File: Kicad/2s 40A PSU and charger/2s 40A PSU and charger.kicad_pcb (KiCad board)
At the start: 4 copper layers, 45 x 20 mm, 117 parts, among them J1 Keystone 3579, J10 USB_C_Receptacle_USB2.0_16P, J11 1.27mm 4 pin socket, J12 USB, J2 JST XH-S Balance Plug, J3 Keystone 3579, J4 Keystone 3569, J5 Keystone 3569, J6 Keystone 3579, J7 Keystone 3579, J8 Keystone 3569, J9 Keystone 3569, Q1 PJA3430, Q2 PJA3430, Q3 Vishay sir404dp, or SiR500DP, Q4 PJA3430, Q5 PJA3430, Q6 Vishay sir404dp, or SiR500DP, U1 BQ76905RGRR, U2 AP63203WU, U3 BQ24780SRUYR, U4 TLV709A33DBVR, U5 THVD1420DRLR, U6 CH32X035G8U6

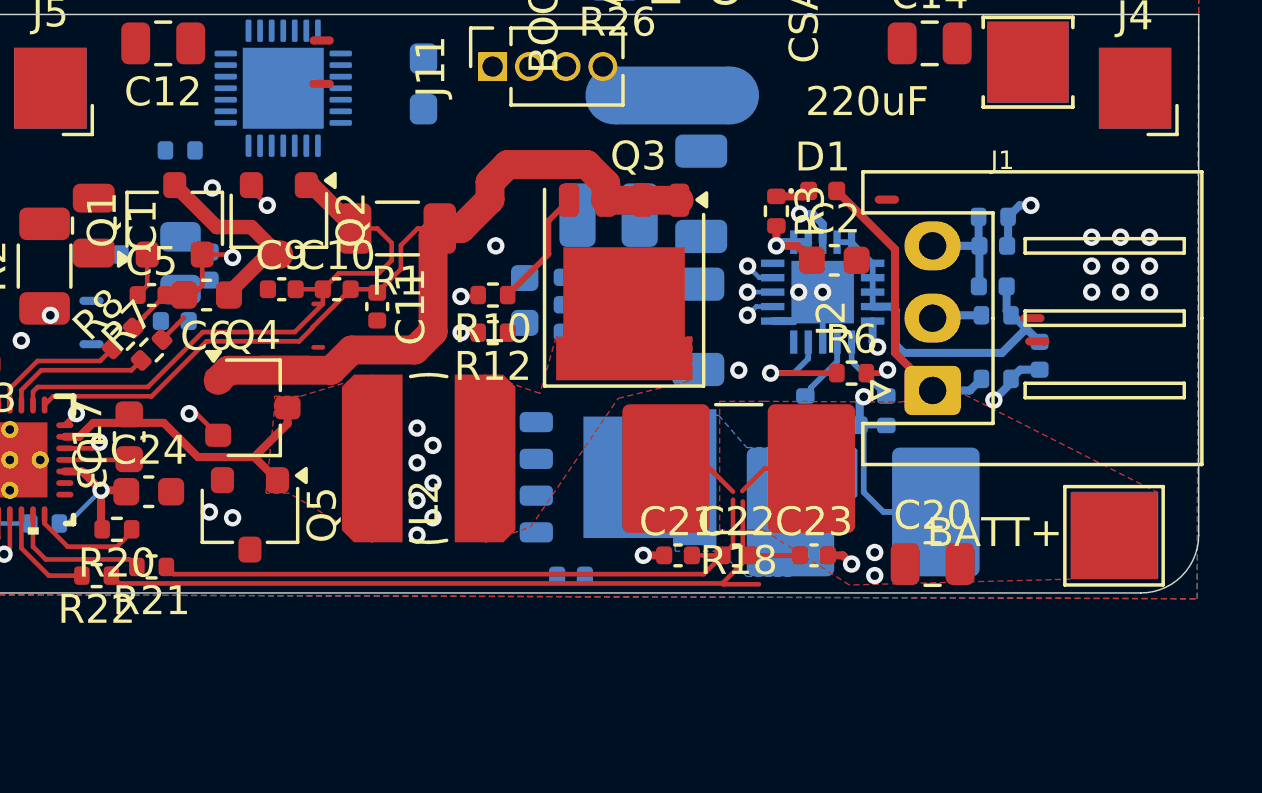
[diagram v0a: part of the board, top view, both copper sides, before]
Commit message: Changed battery input pads to through holes with vias
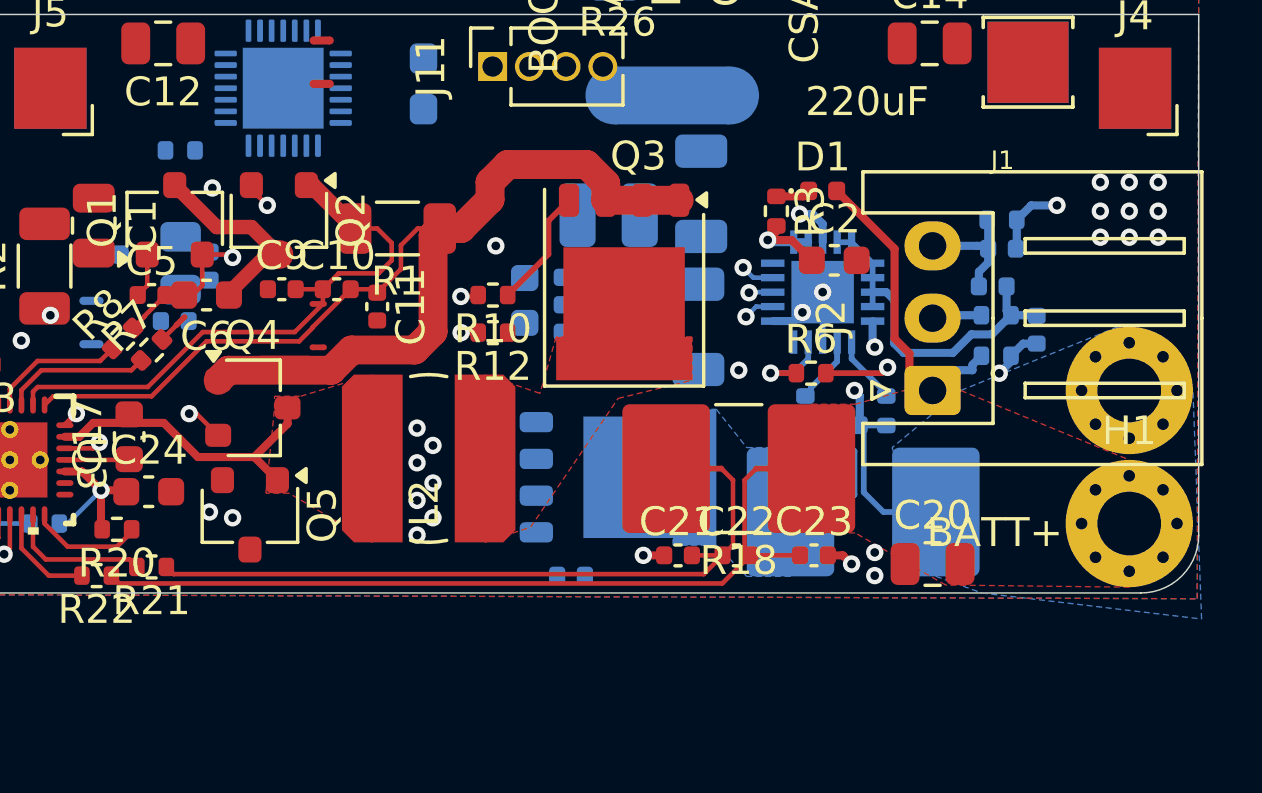
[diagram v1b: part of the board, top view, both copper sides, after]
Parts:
- H1, H2: footprint TestPoint:TestPoint_Pad_3.0x3.0mm -> MountingHole:MountingHole_2.2mm_M2_Pad_Via
- NT14, NT2, NT3, NT5, NT6: footprint custom_Connector:NetTie-2_SMD_Pad0.16mm -> custom_Connector:NetTie-2_SMD_Pad0.2mm
- NT7, NT8: moved to B.Cu
- moved NT9 5.65 mm to (143.1, 124.0), turned to 90 degrees
- moved H2 5.02 mm to (150.7, 125.0), turned to -45 degrees
- moved NT7 3.33 mm to (145.2, 120.0), turned to 180 degrees
- moved NT8 2.71 mm to (145.0, 124.3), turned to 180 degrees
- moved NT5 1.46 mm to (138.0, 127.7), turned to 0 degrees
- moved R6 1.40 mm to (139.7, 124.4)
- moved NT6 1.38 mm to (136.4, 127.7), turned to 180 degrees
- moved C13 0.91 mm to (147.5, 122.9)
- moved R15 0.80 mm to (146.1, 123.8)
- moved H1 0.68 mm to (150.7, 129.6)
- moved C19 0.32 mm to (146.3, 120.1)
- moved R17 0.32 mm to (146.3, 119.1)
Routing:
- net /Battery Balancer/-BAT: track 0.00 -> 23.1 mm, vias 0 -> 1
- net Net-(C18-Pad2): track 25.6 -> 2.87 mm, vias 1 -> 0
- net (no net): track 10.3 -> 0.15 mm
- net Net-(D1-A): track 0.00 -> 6.66 mm
- net /Battery Balancer/+BAT: track 2.72 -> 0.00 mm
- net Net-(Q3-S): track 2.64 -> 0.00 mm
- net Net-(C21-Pad2): track 22.4 -> 24.0 mm
- net /Battery Balancer/Low: track 13.6 -> 15.0 mm
- net Net-(Q6-G): track 0.78 -> 2.22 mm
- net Net-(U1-DSG): track 4.37 -> 2.97 mm
- net Net-(NT8-Pad1): track 0.00 -> 0.63 mm
- net Net-(U1-BAT): track 3.27 -> 3.86 mm
- net /Battery Balancer/Up: track 16.9 -> 17.5 mm
- added copper zone on B.Cu, net /Battery Balancer/-BAT
- added copper zone on B.Cu, net Net-(Q6-S)
- removed copper zone on B.Cu, net (none)

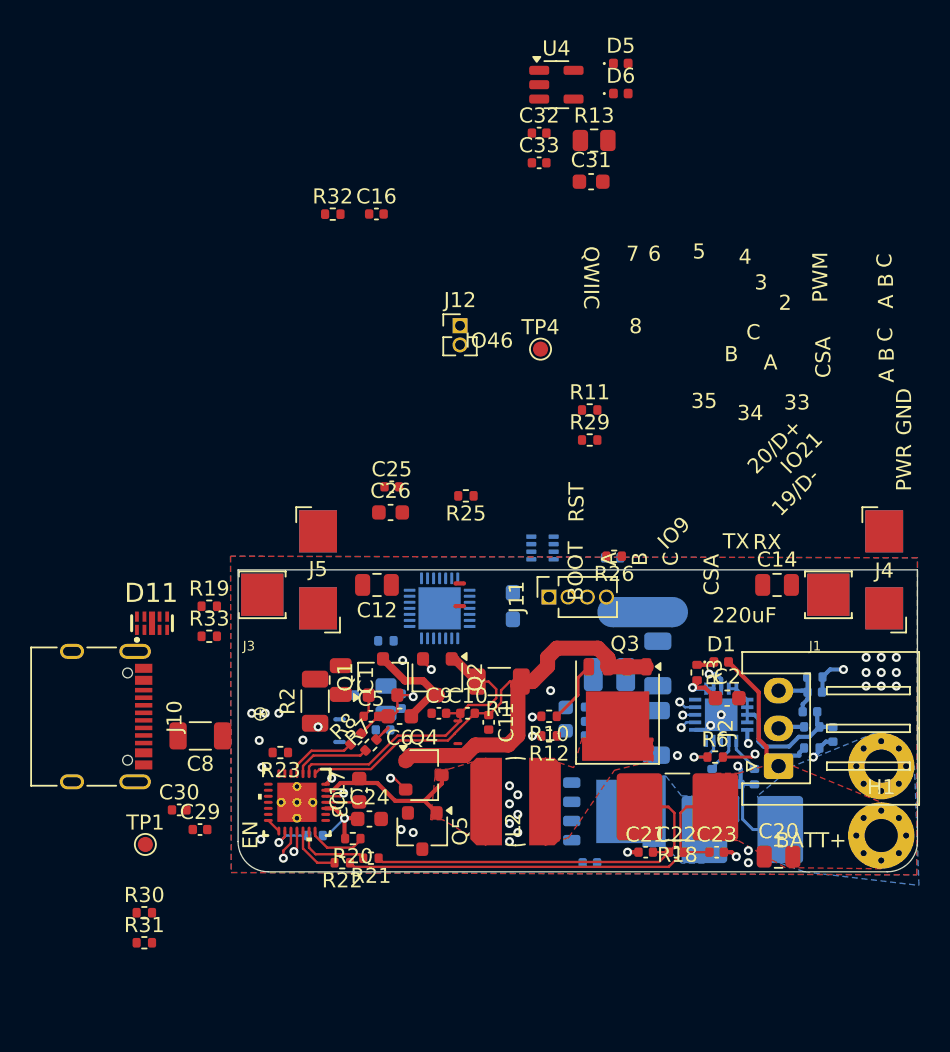
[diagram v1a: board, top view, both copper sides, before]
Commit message: Added TVS diodes for USB-C
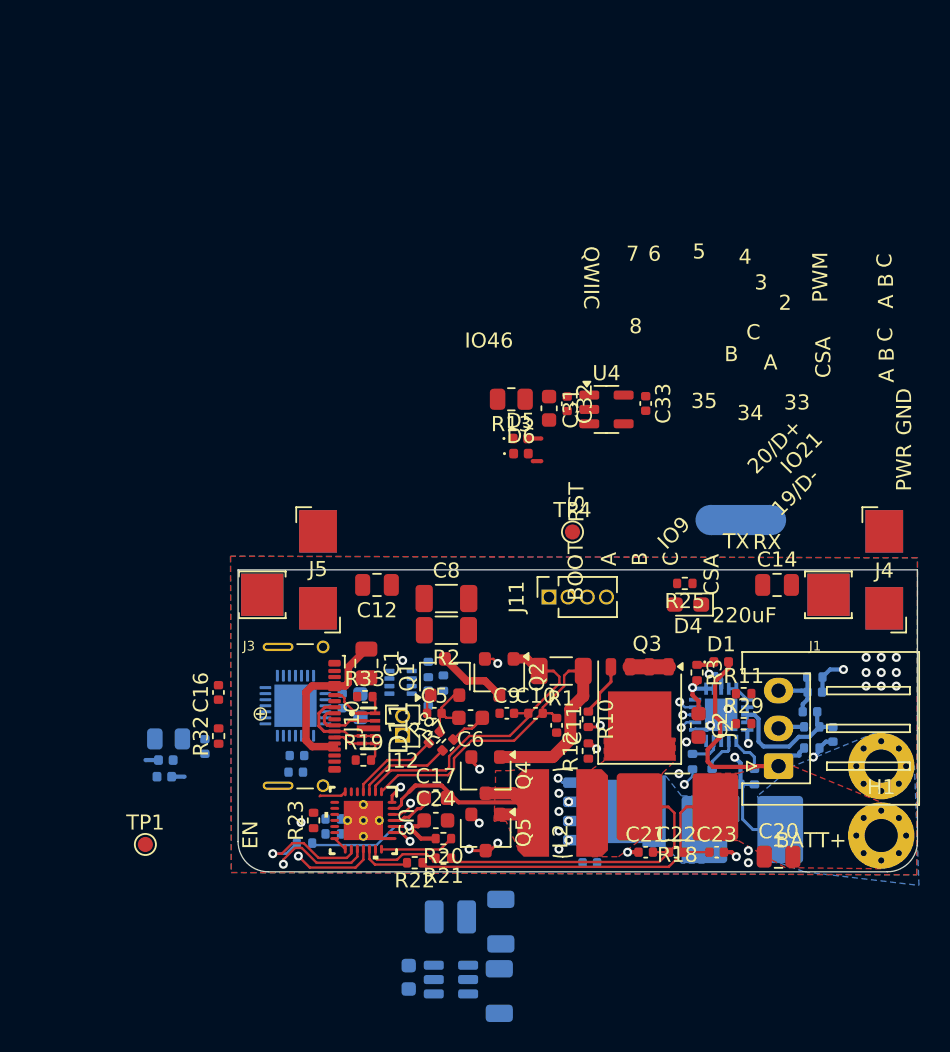
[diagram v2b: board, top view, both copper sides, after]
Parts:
- C25, C26, C29, C30, R26, R30, R31, R6: moved to B.Cu
- D4: moved to F.Cu
- J10: footprint Connector_USB:USB_C_Receptacle_XKB_U262-16XN-4BVC11 -> Connector_USB:USB_C_Receptacle_G-Switch_GT-USB-7025
- moved R32 35.4 mm to (106.8, 123.0), turned to 90 degrees
- moved C16 33.4 mm to (106.8, 120.1), turned to 90 degrees
- moved J12 27.4 mm to (119.0, 123.0), turned to 180 degrees
- moved D5 25.7 mm to (126.8, 103.3)
- moved D6 24.7 mm to (126.8, 104.3)
- moved U4 21.8 mm to (132.5, 101.4)
- moved R11 21.4 mm to (141.6, 120.2)
- moved R29 21.4 mm to (141.6, 122.2)
- moved C27 20.0 mm to (125.5, 135.3)
- moved C28 20.0 mm to (125.4, 139.9)
- moved C40 20.0 mm to (119.4, 139.0)
- moved U2 20.0 mm to (122.2, 139.1)
- moved L3 19.2 mm to (122.2, 135.0)
- moved C8 18.7 mm to (121.9, 113.9), turned to 0 degrees
- moved C32 18.0 mm to (129.9, 101.0), turned to -90 degrees
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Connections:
- D11 pad 2: /Connectors/CC2 -> /Connectors/D-
- D11 pad 4: /Connectors/D- -> /Connectors/D+
- D11 pad 5: /Connectors/D+ -> /Connectors/CC2
- D11 pad 6: /Connectors/D+ -> /Connectors/CC2
- D11 pad 7: /Connectors/D- -> /Connectors/D+
- D11 pad 9: /Connectors/CC2 -> /Connectors/D-
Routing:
- net /Battery Charger/MOTORPWR: track 39.0 -> 2.54 mm
- net Net-(Q2-D): track 20.4 -> 2.02 mm
- net Net-(U3-ACP): track 0.00 -> 17.9 mm
- net Net-(U3-ACN): track 0.00 -> 17.8 mm
- net /Battery Charger/IN: track 1.68 -> 15.9 mm, vias 1 -> 0
- net Net-(U3-BATDRV): track 21.5 -> 30.6 mm
- net Net-(Q6-G): track 2.22 -> 10.8 mm, vias 1 -> 2
- net Net-(Q4-D): track 0.00 -> 8.36 mm
- net Net-(U3-BATSRC): track 23.6 -> 31.9 mm
- net Net-(Q5-G): track 0.00 -> 7.30 mm, vias 0 -> 2
- net Net-(Q4-S): track 10.6 -> 16.9 mm
- net /Connectors/D+: track 0.00 -> 6.05 mm
- net /Battery Charger/REGN: track 5.70 -> 11.5 mm
- net GNDPWR: track 3.94 -> 9.63 mm, vias 30 -> 24
- net Net-(U3-TB_STAT_N): track 3.01 -> 8.18 mm
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
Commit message: Merged Always on PWR for multiple devices
The diode OR and the 10 ohm resistor are now shared between the MCU and the battery charger
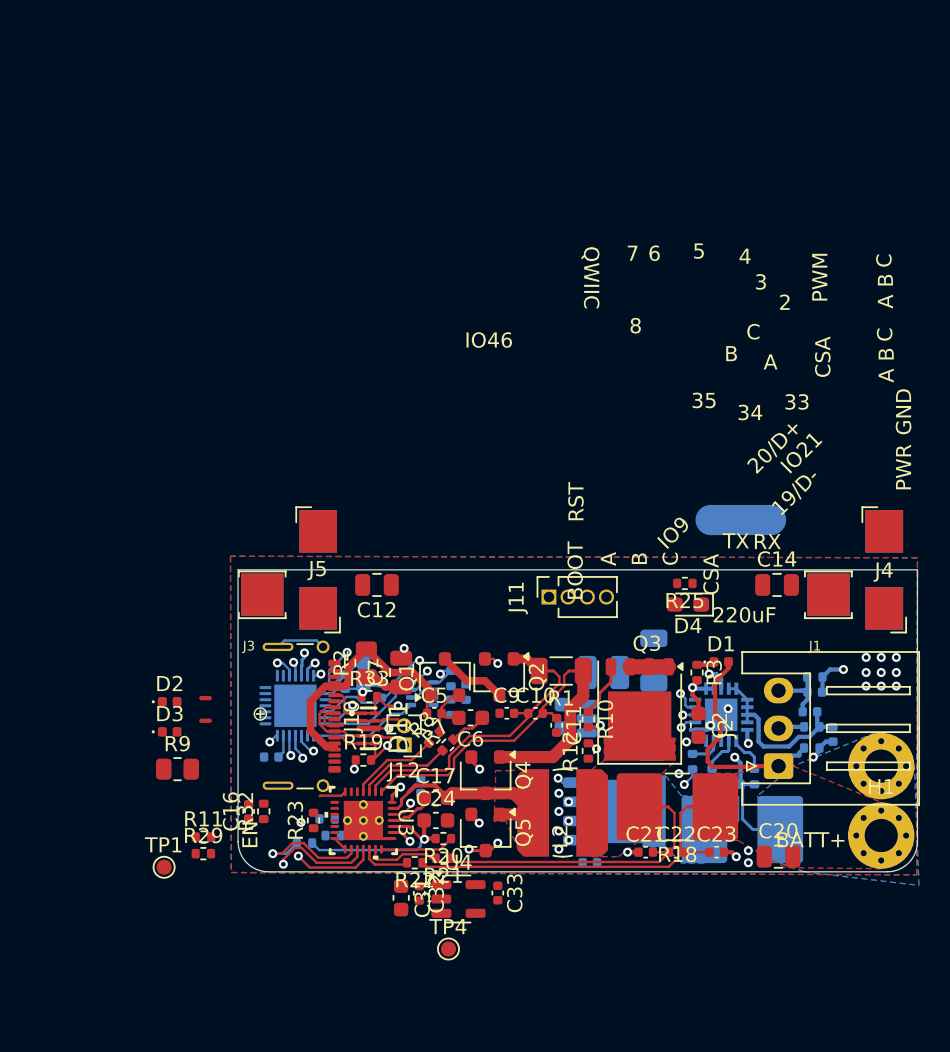
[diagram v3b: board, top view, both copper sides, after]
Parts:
- removed C1: 10uF, 16v, Capacitor_SMD:C_0805_2012Metric
- removed C8: 2.2uf, 16v, Capacitor_SMD:C_1206_3216Metric
- removed D5, D6: GSDH3005, Diode_SMD:D_0402_1005Metric
- removed NT11, NT13: PWR NetTie, custom_Connector:NetTie-2_SMD_Pad0.28mm
- removed R13: 10 ohm, Resistor_SMD:R_0805_2012Metric
- added C7: 10uf, 16v, Capacitor_SMD:C_0805_2012Metric, F.Cu at (118.9, 118.8)
- D2, D3, NT12, R9: moved to F.Cu
- R2: footprint Resistor_SMD:R_1206_3216Metric -> Resistor_SMD:R_0805_2012Metric
- moved R11 37.0 mm to (105.8, 129.7)
- moved R29 36.8 mm to (105.8, 130.8)
- moved C32 33.9 mm to (120.1, 133.4)
- moved U4 33.9 mm to (122.7, 133.8)
- moved C31 33.9 mm to (118.9, 133.7)
- moved C33 33.9 mm to (125.3, 133.4)
- moved TP4 28.8 mm to (122.0, 137.1)
- moved NT10 27.0 mm to (105.9, 120.5), turned to 0 degrees
- moved C27 20.0 mm to (135.6, 118.0)
- moved C28 20.0 mm to (135.5, 122.6)
- moved C40 20.0 mm to (129.5, 121.7)
- moved U2 20.0 mm to (132.3, 121.8)
- moved L3 19.1 mm to (132.3, 118.8)
- moved C15 14.5 mm to (120.2, 126.3)
- moved C16 8.13 mm to (108.8, 128.0)
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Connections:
- C15 pad 1: Net-(U3-VCC) -> /Battery Charger/Always On PWR
- C31 pad 1: Net-(U4-VIN) -> /Battery Charger/Always On PWR
- C32 pad 1: Net-(U4-VIN) -> /Battery Charger/Always On PWR
- NT10 pad 1: Net-(D6-A) -> Net-(D2-A)
- NT12 pad 2: /Battery Balancer/+BAT -> /Battery Charger/MOTORPWR
- R9 pad 1: Net-(U3-VCC) -> /Battery Charger/Always On PWR
- U3 pad 28: Net-(U3-VCC) -> /Battery Charger/Always On PWR
- U4 pad 1: Net-(U4-VIN) -> /Battery Charger/Always On PWR
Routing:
- net GND: track 1.66 -> 10.4 mm, vias 2 -> 6
- net /Battery Charger/Charger IADP: track 1.82 -> 10.0 mm, vias 0 -> 1
- net /MCU/UART1_RX: track 0.00 -> 7.30 mm
- net /MCU/UART1_TX: track 0.00 -> 7.15 mm
- net /Connectors/CC2: track 4.07 -> 8.49 mm, vias 0 -> 2
- net /Battery Charger/IN: track 15.9 -> 20.3 mm
- net /MCU/UART1-RTS: track 0.00 -> 4.03 mm, vias 0 -> 2
- net /Connectors/D-: track 4.74 -> 8.45 mm, vias 0 -> 1
- net /MCU/3.3v: track 0.00 -> 3.64 mm
- net Net-(Q1-G): track 12.2 -> 8.82 mm
- net Net-(J10-SHIELD): track 0.00 -> 3.33 mm
- net /Connectors/D+: track 6.05 -> 9.12 mm, vias 0 -> 1
- net Net-(C7-Pad1): track 0.00 -> 2.58 mm, vias 1 -> 0
- net /Connectors/CC1: track 4.49 -> 7.00 mm, vias 0 -> 2
- net Net-(Q4-S): track 16.9 -> 14.8 mm
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
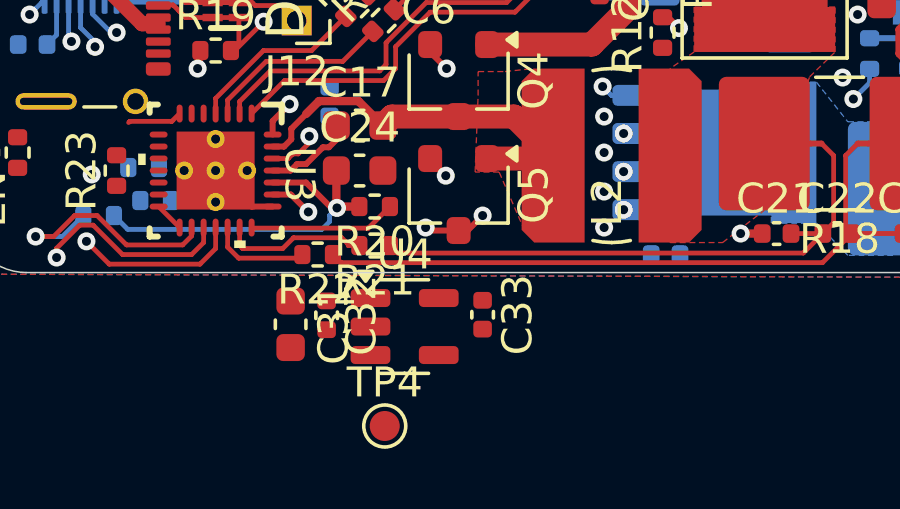
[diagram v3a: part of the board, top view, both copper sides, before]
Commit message: Switched out always on 3v3 reg to smaller WSON-6
This is more expensive, but a bit smaller and still has the same input voltage range
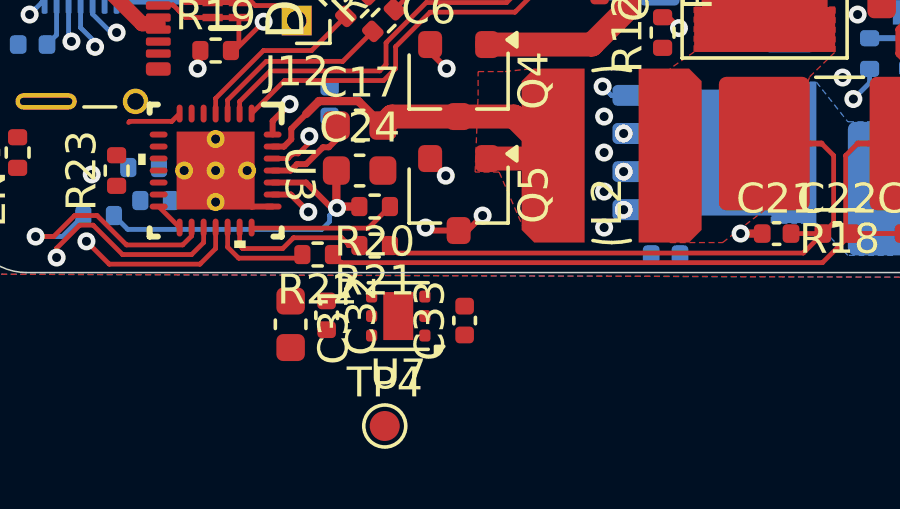
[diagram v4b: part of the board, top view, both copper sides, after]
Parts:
- removed U4: TLV709A33DBVR, Package_TO_SOT_SMD:SOT-23-5
- added U7: TPS7A2633DRV, Package_SON:WSON-6-1EP_2x2mm_P0.65mm_EP1x1.6mm, F.Cu at (122.5, 133.4)
- moved C33 0.63 mm to (124.7, 133.6), turned to 90 degrees
